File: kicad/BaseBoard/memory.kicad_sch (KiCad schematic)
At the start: 4 parts, among them U7 62256, U8 28C256

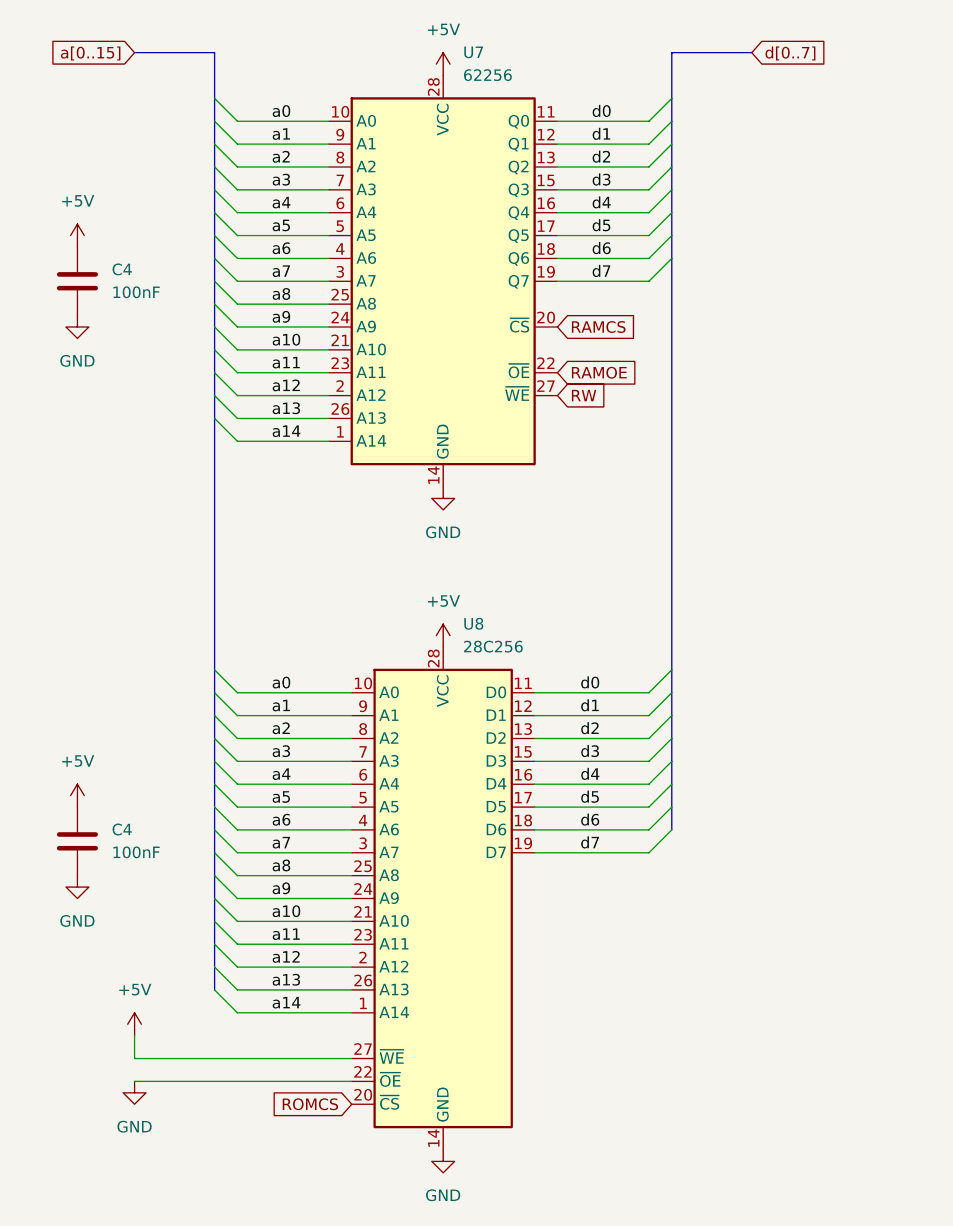
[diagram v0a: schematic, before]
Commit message: I/O board schematic and layout
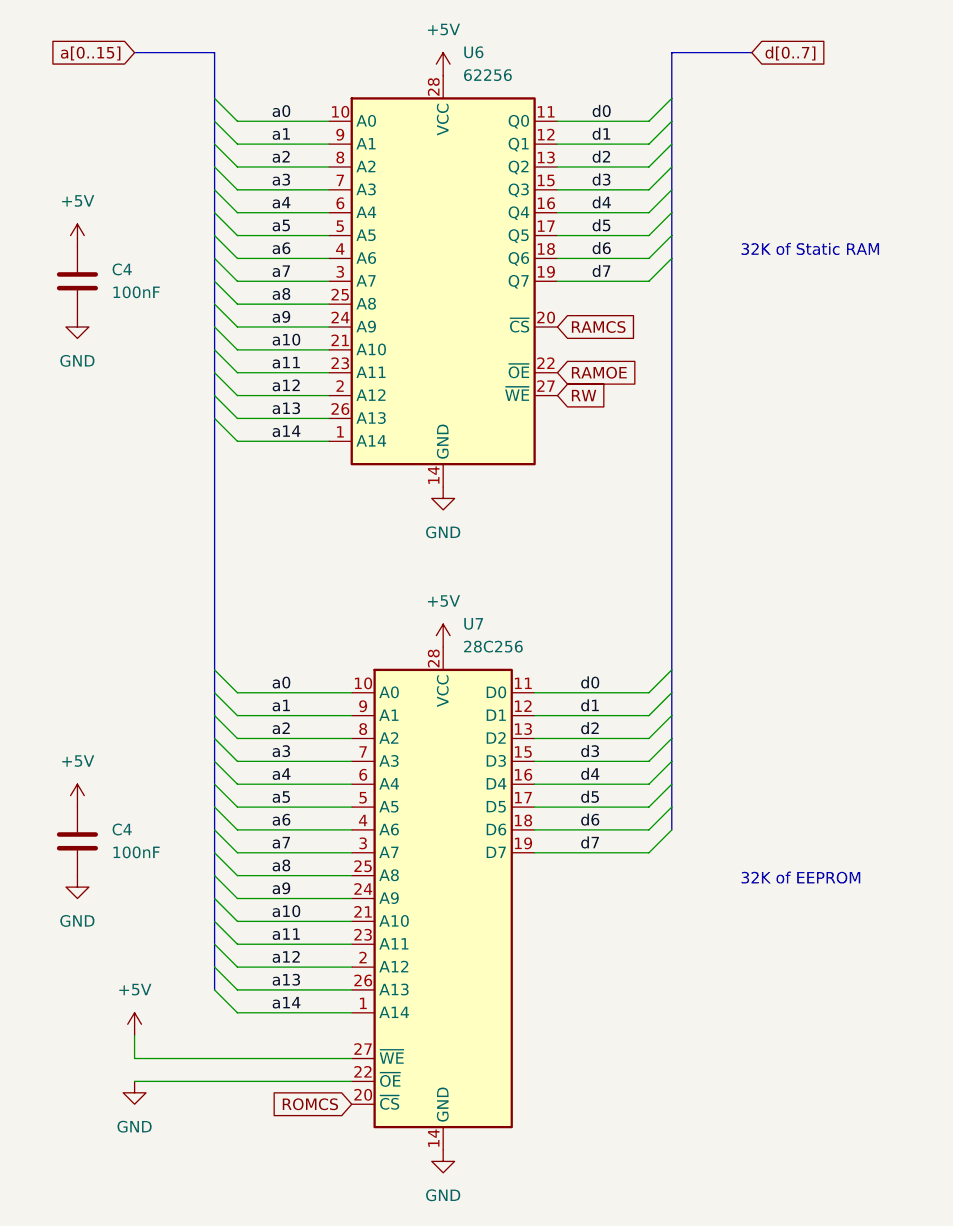
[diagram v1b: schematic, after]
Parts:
- renumbered U7 to U6, U8 to U7
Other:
- note added: "32K of EEPROM"
- note added: "32K of Static RAM"
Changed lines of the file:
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@@
     (stroke (width 0) (type default))
+  )
+  (text "32K of EEPROM" (at 180.34 134.62 0)
+    (effects (font (size 1.27 1.27)) (justify left bottom))
+  )
+  (text "32K of Static RAM" (at 180.34 64.77 0)
+    (effects (font (size 1.27 1.27)) (justify left bottom))
   )
   (label "a7" (at 128.27 67.31 0) (fields_autoplaced)
@@
   (symbol (lib_id "power:GND") (at 113.03 156.21 0) (unit 1)
     (in_bom yes) (on_board yes) (dnp no) (fields_autoplaced)
-    (property "Reference" "#PWR048" (at 113.03 162.56 0)
+    (property "Reference" "#PWR046" (at 113.03 162.56 0)
       (effects (font (size 1.27 1.27)) hide)
     )
@@
       (project "MiniComputerBase"
         (path "/3f118084-1458-40be-b12b-e8391c9e712b/66b9f355-b8e4-43cb-823d-08b79a35e03a"
-          (reference "#PWR048") (unit 1)
+          (reference "#PWR046") (unit 1)
         )
       )
@@
         )
         (path "/3f118084-1458-40be-b12b-e8391c9e712b/66b9f355-b8e4-43cb-823d-08b79a35e03a"
-          (reference "#PWR043") (unit 1)
+          (reference "#PWR041") (unit 1)
         )
       )
@@
   (symbol (lib_id "Memory_EEPROM:28C256") (at 147.32 135.89 0) (unit 1)
     (in_bom yes) (on_board yes) (dnp no) (fields_autoplaced)
-    (property "Reference" "U8" (at 149.5141 105.41 0)
+    (property "Reference" "U7" (at 149.5141 105.41 0)
       (effects (font (size 1.27 1.27)) (justify left))
     )
@@
       (project "MiniComputerBase"
         (path "/3f118084-1458-40be-b12b-e8391c9e712b/66b9f355-b8e4-43cb-823d-08b79a35e03a"
-          (reference "U8") (unit 1)
+          (reference "U7") (unit 1)
         )
       )
@@
   (symbol (lib_id "power:+5V") (at 147.32 107.95 0) (unit 1)
     (in_bom yes) (on_board yes) (dnp no) (fields_autoplaced)
-    (property "Reference" "#PWR051" (at 147.32 111.76 0)
+    (property "Reference" "#PWR049" (at 147.32 111.76 0)
       (effects (font (size 1.27 1.27)) hide)
     )
@@
       (project "MiniComputerBase"
         (path "/3f118084-1458-40be-b12b-e8391c9e712b/66b9f355-b8e4-43cb-823d-08b79a35e03a"
-          (reference "#PWR051") (unit 1)
+          (reference "#PWR049") (unit 1)
         )
       )
@@
         )
         (path "/3f118084-1458-40be-b12b-e8391c9e712b/66b9f355-b8e4-43cb-823d-08b79a35e03a"
-          (reference "#PWR045") (unit 1)
+          (reference "#PWR043") (unit 1)
         )
       )
@@
         )
         (path "/3f118084-1458-40be-b12b-e8391c9e712b/66b9f355-b8e4-43cb-823d-08b79a35e03a"
-          (reference "#PWR044") (unit 1)
+          (reference "#PWR042") (unit 1)
         )
       )
@@
   (symbol (lib_id "Memory_RAM:CY62256-70PC") (at 147.32 67.31 0) (unit 1)
     (in_bom yes) (on_board yes) (dnp no) (fields_autoplaced)
-    (property "Reference" "U7" (at 149.5141 41.91 0)
+    (property "Reference" "U6" (at 149.5141 41.91 0)
       (effects (font (size 1.27 1.27)) (justify left))
     )
@@
       (project "MiniComputerBase"
         (path "/3f118084-1458-40be-b12b-e8391c9e712b/66b9f355-b8e4-43cb-823d-08b79a35e03a"
-          (reference "U7") (unit 1)
+          (reference "U6") (unit 1)
         )
       )
@@
   (symbol (lib_id "power:+5V") (at 113.03 151.13 0) (unit 1)
     (in_bom yes) (on_board yes) (dnp no) (fields_autoplaced)
-    (property "Reference" "#PWR047" (at 113.03 154.94 0)
+    (property "Reference" "#PWR045" (at 113.03 154.94 0)
       (effects (font (size 1.27 1.27)) hide)
     )
@@
       (project "MiniComputerBase"
         (path "/3f118084-1458-40be-b12b-e8391c9e712b/66b9f355-b8e4-43cb-823d-08b79a35e03a"
-          (reference "#PWR047") (unit 1)
+          (reference "#PWR045") (unit 1)
         )
       )
@@
   (symbol (lib_id "power:GND") (at 147.32 163.83 0) (unit 1)
     (in_bom yes) (on_board yes) (dnp no) (fields_autoplaced)
-    (property "Reference" "#PWR052" (at 147.32 170.18 0)
+    (property "Reference" "#PWR050" (at 147.32 170.18 0)
       (effects (font (size 1.27 1.27)) hide)
     )
@@
       (project "MiniComputerBase"
         (path "/3f118084-1458-40be-b12b-e8391c9e712b/66b9f355-b8e4-43cb-823d-08b79a35e03a"
-          (reference "#PWR052") (unit 1)
+          (reference "#PWR050") (unit 1)
         )
       )
@@
         )
         (path "/3f118084-1458-40be-b12b-e8391c9e712b/66b9f355-b8e4-43cb-823d-08b79a35e03a"
-          (reference "#PWR046") (unit 1)
+          (reference "#PWR044") (unit 1)
         )
       )
@@
   (symbol (lib_id "power:GND") (at 147.32 90.17 0) (unit 1)
     (in_bom yes) (on_board yes) (dnp no) (fields_autoplaced)
-    (property "Reference" "#PWR050" (at 147.32 96.52 0)
+    (property "Reference" "#PWR048" (at 147.32 96.52 0)
       (effects (font (size 1.27 1.27)) hide)
     )
@@
       (project "MiniComputerBase"
         (path "/3f118084-1458-40be-b12b-e8391c9e712b/66b9f355-b8e4-43cb-823d-08b79a35e03a"
-          (reference "#PWR050") (unit 1)
+          (reference "#PWR048") (unit 1)
         )
       )
@@
   (symbol (lib_id "power:+5V") (at 147.32 44.45 0) (unit 1)
     (in_bom yes) (on_board yes) (dnp no) (fields_autoplaced)
-    (property "Reference" "#PWR049" (at 147.32 48.26 0)
+    (property "Reference" "#PWR047" (at 147.32 48.26 0)
       (effects (font (size 1.27 1.27)) hide)
     )
@@
       (project "MiniComputerBase"
         (path "/3f118084-1458-40be-b12b-e8391c9e712b/66b9f355-b8e4-43cb-823d-08b79a35e03a"
-          (reference "#PWR049") (unit 1)
-        )
-      )
+          (reference "#PWR047") (unit 1)
+        )
+      )
